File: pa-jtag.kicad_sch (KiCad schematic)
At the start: 25 parts, among them J1 USB_B, J2 JTAG, J3 VCCIO, J4 VOUT, U1 FT232RL, U2 L78L33_TO92

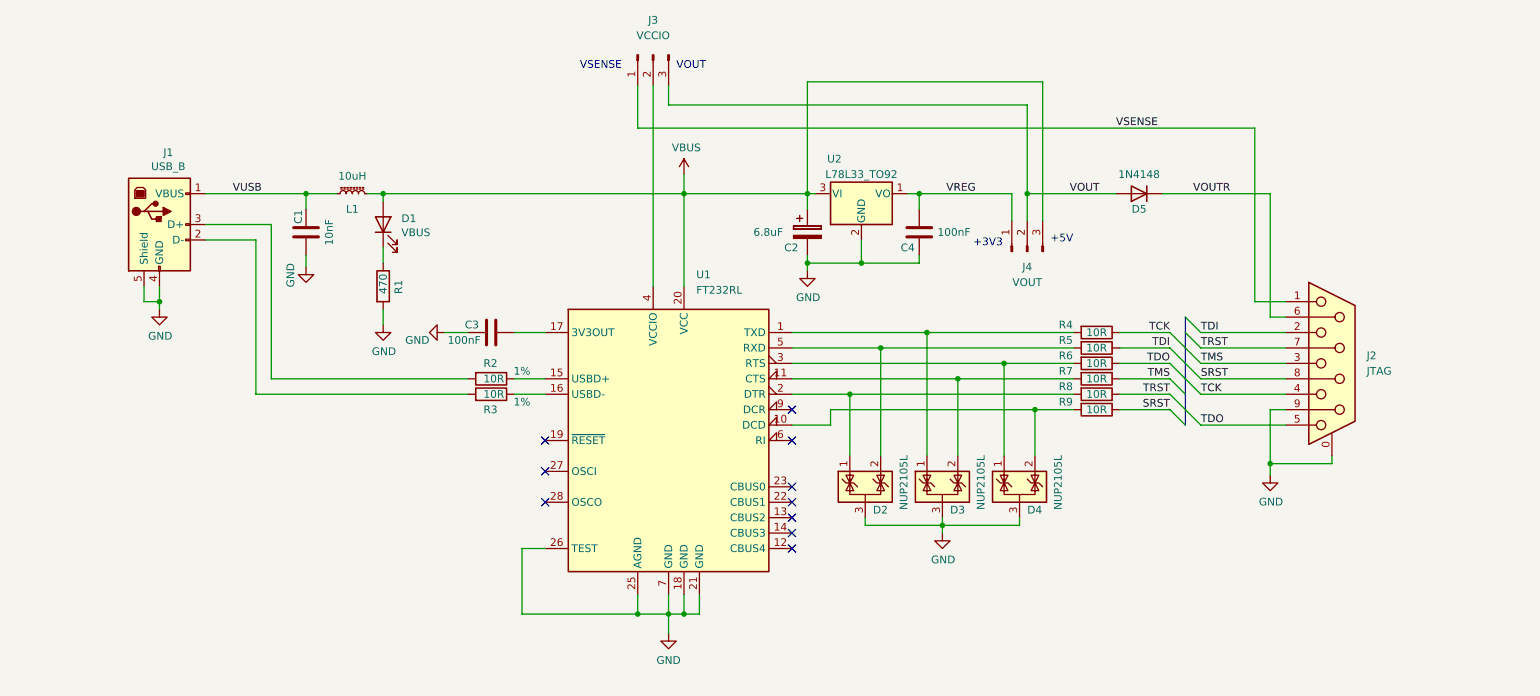
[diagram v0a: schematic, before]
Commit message: Add J5 and Open Drain Resets
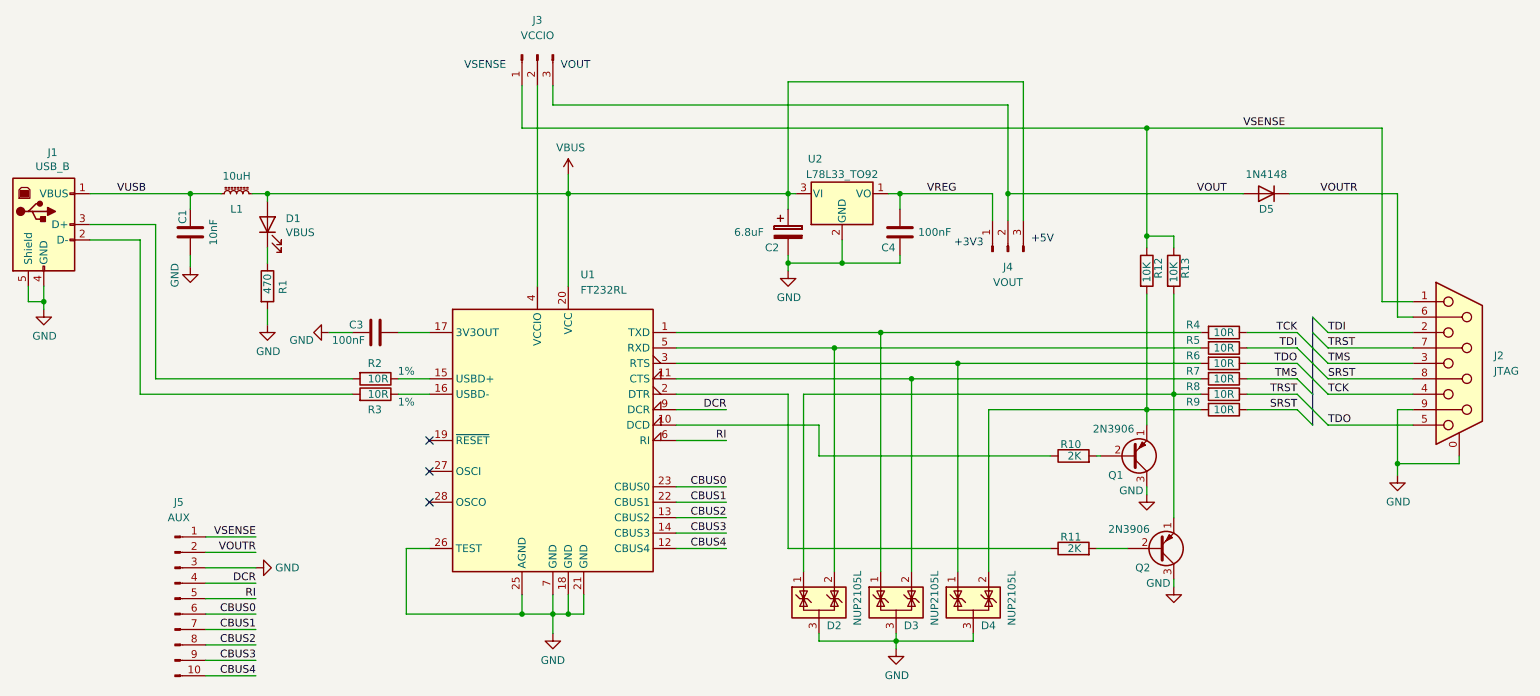
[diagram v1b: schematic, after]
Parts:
- added J5: AUX, Connector_PinHeader_2.54mm:PinHeader_2x05_P2.54mm_Vertical, symbol Connector:Conn_01x10_Male
- added Q1, Q2: 2N3906, Package_TO_SOT_THT:TO-92_Inline, symbol Transistor_BJT:2N3906
- added R10, R11: 2K, Resistor_SMD:R_0603_1608Metric, symbol Device:R
- added R12, R13: 10K, Resistor_SMD:R_0603_1608Metric, symbol Device:R
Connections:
- net GND: now also J5.3 (Pin_3), Q1.3 (C), Q2.3 (C)
- net VOUTR: now also J5.2 (Pin_2)
- net VSENSE: now also J5.1 (Pin_1), R12.1, R13.1
- net at D4.2 (K), R9.2: now also Q1.1 (E), R12.2; no longer U1.10 (DCD)
- net at D2.1 (K), R8.2: now also Q2.1 (E), R13.2; no longer U1.2 (DTR)
- net CBUS4: now reaches U1.12 (CBUS4)
- net CBUS4: now also J5.10 (Pin_10)
- net CBUS2: now reaches U1.13 (CBUS2)
- net CBUS2: now also J5.8 (Pin_8)
- net CBUS3: now reaches U1.14 (CBUS3)
- net CBUS3: now also J5.9 (Pin_9)
- net CBUS1: now reaches U1.22 (CBUS1)
- net CBUS1: now also J5.7 (Pin_7)
- net CBUS0: now reaches U1.23 (CBUS0)
- net CBUS0: now also J5.6 (Pin_6)
- net RI: now reaches U1.6 (RI)
- net RI: now also J5.5 (Pin_5)
- net DCR: now reaches U1.9 (DCR)
- net DCR: now also J5.4 (Pin_4)
- new net: R11.1, U1.2 (DTR)
- new net: Q2.2 (B), R11.2
- new net: R10.1, U1.10 (DCD)
- new net: Q1.2 (B), R10.2
- no-connect marks 10 -> 3
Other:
- moved on the sheet: C1, C2, C3, C4, D1, D2, D3, D4, D5, J1, J2, J3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

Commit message: ch32 initial commit
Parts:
- added C? (x4): 100nF, Capacitor_SMD:C_0603_1608Metric, symbol Device:C
- added U?: MAX3232, symbol Interface_UART:MAX3232
- added U?: CH32V103C8T6, Package_QFP:LQFP-48_7x7mm_P0.5mm, symbol MCU_ST_STM32F1:STM32F103C8Tx
- J2: value JTAG -> RS232
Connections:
- net CBUS0: no longer U1.23 (CBUS0)
- net CBUS1: no longer U1.22 (CBUS1)
- net CBUS2: no longer U1.13 (CBUS2)
- net CBUS3: no longer U1.14 (CBUS3)
- net CBUS4: no longer U1.12 (CBUS4)
- net DCR: no longer U1.9 (DCR)
- net GND: now also C?.2, C?.2, C?.2, C?.2, U?.23 (VSS), U?.35 (VSS), U?.47 (VSS), U?.8 (VSSA); no longer J2.0 (PAD), J2.9, U1.18 (GND), U1.21 (GND), U1.25 (AGND), U1.26 (TEST), U1.7 (GND)
- net RI: no longer U1.6 (RI)
- net SRST: no longer J2.8
- net TCK: no longer J2.4
- net TDI: no longer J2.2
- net TDO: no longer J2.5
- net TMS: no longer J2.3
- net TRST: no longer J2.7
- net VBUS: now also C3.1, C?.1, C?.1, C?.1, C?.1, U?.1 (VBAT), U?.24 (VDD), U?.36 (VDD), U?.48 (VDD), U?.9 (VDDA); no longer U1.20 (VCC)
- net VOUTR: no longer J2.6
- net VSENSE: no longer J2.1
- net at D3.1 (K), R4.2: no longer U1.1 (TXD)
- net at D3.2 (K), R7.2: no longer U1.11 (CTS)
- net at D4.1 (K), R6.2: no longer U1.3 (RTS)
- net at D2.2 (K), R5.2: no longer U1.5 (RXD)
- net at U1.17 (3V3OUT): no longer C3.1
- net at R2.1: no longer U1.15 (USBD+)
- net at R3.1: no longer U1.16 (USBD-)
- net at R11.1: no longer U1.2 (DTR)
- net at U1.4 (VCCIO): no longer J3.2 (Pin_2)
- net at R10.1: no longer U1.10 (DCD)
- new net VCCIO: J3.2 (Pin_2)
- no-connect marks 3 -> 0
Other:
- note added: "LEVEL SHIFTER"
- moved on the sheet: C1, C2, C3, C4, D1, D2, D3, D4, D5, J1, J2, J3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

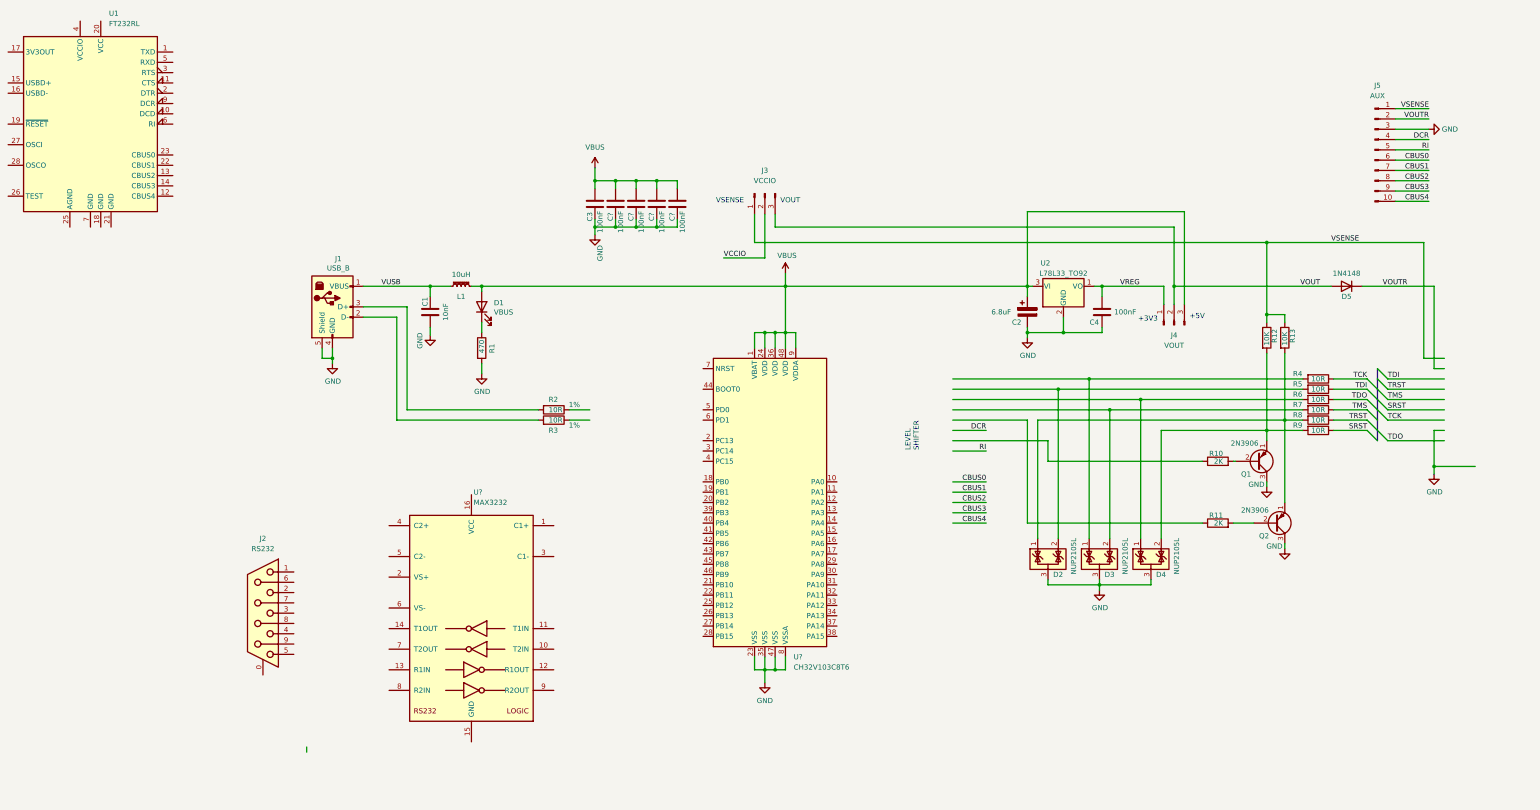
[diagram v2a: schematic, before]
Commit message: ch32v103 jtag schematic
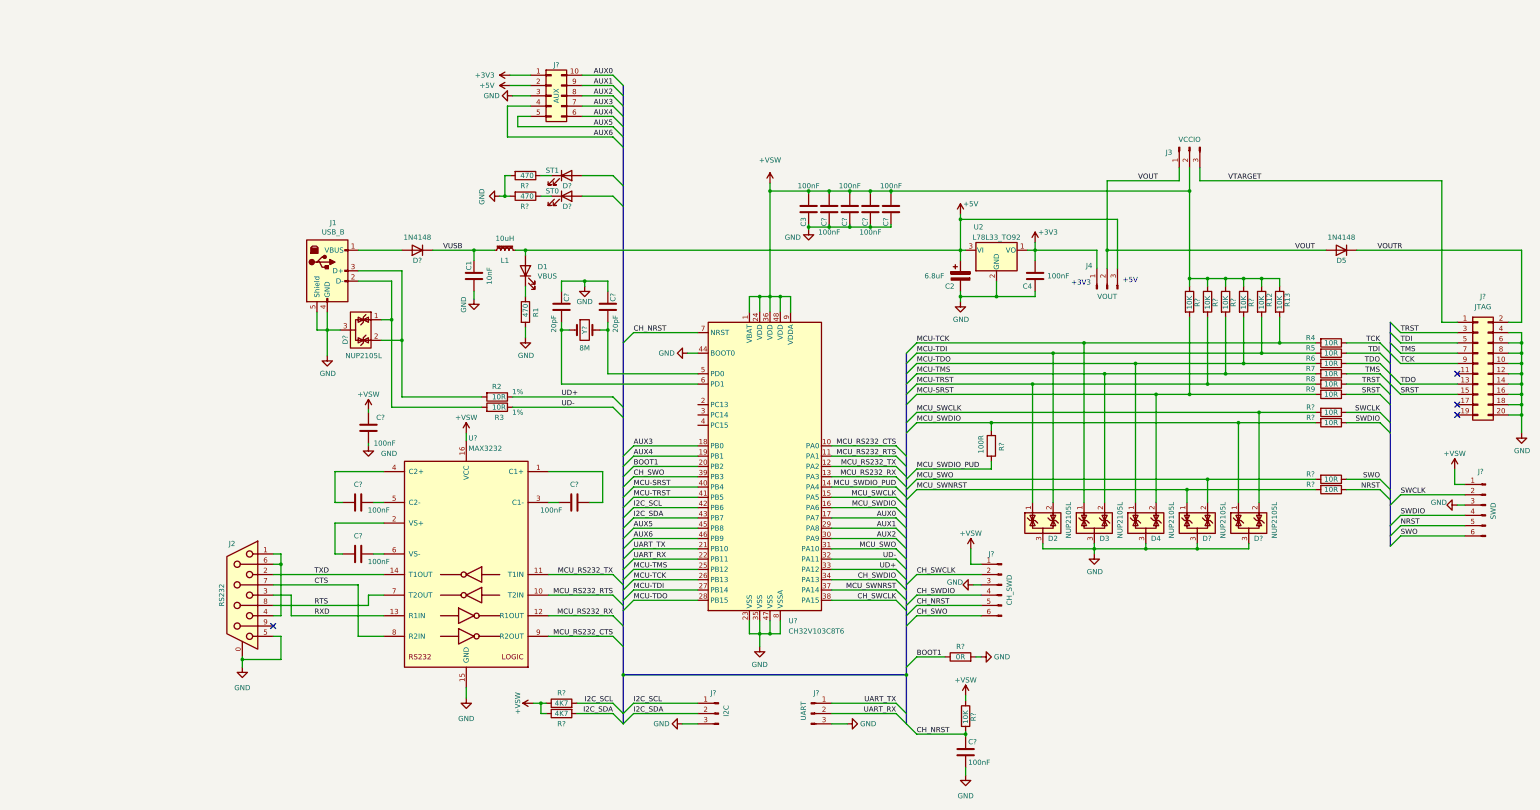
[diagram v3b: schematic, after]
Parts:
- removed J5: AUX, Connector_PinHeader_2.54mm:PinHeader_2x05_P2.54mm_Vertical, symbol Connector:Conn_01x10_Male
- removed Q1, Q2: 2N3906, Package_TO_SOT_THT:TO-92_Inline, symbol Transistor_BJT:2N3906
- removed R10, R11: 2K, Resistor_SMD:R_0603_1608Metric, symbol Device:R
- removed U1: FT232RL, Package_SO:SSOP-28_5.3x10.2mm_P0.65mm, symbol Interface_USB:FT232RL
- added C? (x5): 100nF, symbol Device:C
- added C? (x2): 20pF, symbol Device:C
- added D? (x3): NUP2105L, Package_TO_SOT_SMD:SOT-23, symbol Power_Protection:NUP2105L
- added D?: ST1, LED_SMD:LED_0603_1608Metric, symbol Device:LED
- added D?: 1N4148, Diode_SMD:D_MiniMELF, symbol Device:D
- added D?: ST0, LED_SMD:LED_0603_1608Metric, symbol Device:LED
- added J?: UART, symbol Connector:Conn_01x03_Male
- added J?: I2C, symbol Connector:Conn_01x03_Male
- added J?: CH_SWD, symbol Connector:Conn_01x06_Male
- added J?: AUX, symbol Connector_Generic:Conn_02x05_Counter_Clockwise
- added J?: SWD, symbol Connector:Conn_01x06_Male
- added J?: JTAG, symbol Connector_Generic:Conn_02x10_Odd_Even
- added R? (x2): 470, Resistor_SMD:R_0603_1608Metric, symbol Device:R
- added R?: 100R, symbol Device:R
- added R?: 0R, symbol Device:R
- added R? (x2): 4K7, symbol Device:R
- added R? (x4): 10R, Resistor_SMD:R_0603_1608Metric, symbol Device:R
- added R? (x4): 10K, Resistor_SMD:R_0603_1608Metric, symbol Device:R
- added R?: 10K, symbol Device:R
- added Y?: 8M, symbol Device:Crystal
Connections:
- net VCCIO is gone; now on net +VSW: J3.2 (Pin_2)
- net GND: now also J2.0 (PAD), J2.5, U?.15 (GND), U?.44 (BOOT0), C?.1, C?.1, C?.2, C?.2, D?.3 (A), D?.3 (A), D?.3 (A), J?.10 (Pin_10), J?.12 (Pin_12), J?.14 (Pin_14), J?.16 (Pin_16), J?.18 (Pin_18), J?.20 (Pin_20), J?.3 (Pin_3), J?.3 (Pin_3), J?.3 (Pin_3), J?.3 (Pin_3), J?.3 (Pin_3), J?.4 (Pin_4), J?.6 (Pin_6), J?.8 (Pin_8), R?.2, R?.2, R?.2
- net SRST: now also J?.15 (Pin_15)
- net TCK: now also J?.9 (Pin_9)
- net TDI: now also J?.5 (Pin_5)
- net TDO: now also J?.13 (Pin_13)
- net TMS: now also J?.7 (Pin_7)
- net TRST: now also J?.3 (Pin_3)
- net VOUT: now also J3.1 (Pin_1); no longer J3.3 (Pin_3)
- net VOUTR: now also J?.2 (Pin_2)
- net VUSB: now also D?.1 (K); no longer J1.1 (VBUS)
- net MCU-TCK: now reaches D3.1 (K), R4.2
- net MCU-TCK: now also R13.2, U?.26 (PB13)
- net MCU-TMS: now reaches D3.2 (K), R7.2
- net MCU-TMS: now also U?.25 (PB12), R?.2
- net at J1.2 (D-), R3.2: now also D?.1 (K)
- net at J1.3 (D+), R2.2: now also D?.2 (K)
- net MCU-TDO: now reaches D4.1 (K), R6.2
- net MCU-TDO: now also U?.28 (PB15), R?.2
- net MCU-SRST: now reaches D4.2 (K), R9.2
- net MCU-SRST: now also U?.40 (PB4), R?.2; no longer R12.2
- net MCU-TRST: now reaches D2.1 (K), R8.2
- net MCU-TRST: now also U?.41 (PB5), R?.2; no longer R13.2
- net MCU-TDI: now reaches D2.2 (K), R5.2
- net MCU-TDI: now also R12.2, U?.27 (PB14)
- net UD+: now reaches R2.1
- net UD+: now also U?.33 (PA12)
- net UD-: now reaches R3.1
- net UD-: now also U?.32 (PA11)
- net at U?.1 (C1+): now also C?.2
- net MCU_RS232_RTS: now reaches U?.10 (T2IN)
- net MCU_RS232_RTS: now also U?.11 (PA1)
- net MCU_RS232_TX: now reaches U?.11 (T1IN)
- net MCU_RS232_TX: now also U?.12 (PA2)
- net MCU_RS232_RX: now reaches U?.12 (R1OUT)
- net MCU_RS232_RX: now also U?.13 (PA3)
- net RXD: now reaches U?.13 (R1IN)
- net RXD: now also J2.3
- net TXD: now reaches U?.14 (T1OUT)
- net TXD: now also J2.2
- net +VSW: now reaches U?.16 (VCC)
- net +VSW: now also C3.1, C?.1, C?.1, C?.1, C?.1, R12.1, R13.1, U?.1 (VBAT), U?.24 (VDD), U?.36 (VDD), U?.48 (VDD), U?.9 (VDDA), C?.1, J?.1 (Pin_1), J?.1 (Pin_1), R?.1, R?.1, R?.1, R?.1, R?.1, R?.1, R?.1
- net at U?.2 (VS+): now also C?.1
- net at U?.3 (C1-): now also C?.1
- net at U?.4 (C2+): now also C?.1
- net at U?.5 (C2-): now also C?.2
- net at U?.6 (VS-): now also C?.2
- net RTS: now reaches U?.7 (T2OUT)
- net RTS: now also J2.8
- net CTS: now reaches U?.8 (R2IN)
- net CTS: now also J2.7
- net MCU_RS232_CTS: now reaches U?.9 (R2OUT)
- net MCU_RS232_CTS: now also U?.10 (PA0)
- net at J2.1: now also J2.4, J2.6
- net MCU_SWDIO_PUD: now reaches U?.14 (PA4)
- net MCU_SWDIO_PUD: now also R?.2
- net MCU_SWCLK: now reaches U?.15 (PA5)
- net MCU_SWCLK: now also D?.2 (K), R?.2
- net MCU_SWDIO: now reaches U?.16 (PA6)
- net MCU_SWDIO: now also D?.1 (K), R?.1, R?.2
- net AUX0: now reaches U?.17 (PA7)
- net AUX0: now also J?.10 (Pin_10)
- net AUX3: now reaches U?.18 (PB0)
- net AUX3: now also J?.7 (Pin_7)
- net AUX4: now reaches U?.19 (PB1)
- net AUX4: now also J?.6 (Pin_6)
- net BOOT1: now reaches U?.20 (PB2)
- net BOOT1: now also R?.1
- net UART_TX: now reaches U?.21 (PB10)
- net UART_TX: now also J?.1 (Pin_1)
- net UART_RX: now reaches U?.22 (PB11)
- net UART_RX: now also J?.2 (Pin_2)
- net AUX1: now reaches U?.29 (PA8)
- net AUX1: now also J?.9 (Pin_9)
- net AUX2: now reaches U?.30 (PA9)
- net AUX2: now also J?.8 (Pin_8)
- net MCU_SWO: now reaches U?.31 (PA10)
- net MCU_SWO: now also D?.2 (K), R?.2
- net CH_SWDIO: now reaches U?.34 (PA13)
- net CH_SWDIO: now also J?.4 (Pin_4)
- net MCU_SWNRST: now reaches U?.37 (PA14)
- net MCU_SWNRST: now also D?.1 (K), R?.2
- net CH_SWCLK: now reaches U?.38 (PA15)
- net CH_SWCLK: now also J?.2 (Pin_2)
- net CH_SWO: now reaches U?.39 (PB3)
- net CH_SWO: now also J?.6 (Pin_6)
- net I2C_SCL: now reaches U?.42 (PB6)
- net I2C_SCL: now also J?.1 (Pin_1), R?.2
- net I2C_SDA: now reaches U?.43 (PB7)
- net I2C_SDA: now also J?.2 (Pin_2), R?.2
- net AUX5: now reaches U?.45 (PB8)
- net AUX5: now also J?.5 (Pin_5)
- net AUX6: now reaches U?.46 (PB9)
- net AUX6: now also J?.4 (Pin_4)
- net at U?.5 (PD0): now also C?.2, Y?.2
- net at U?.6 (PD1): now also C?.2, Y?.1
- net CH_NRST: now reaches U?.7 (NRST)
- net CH_NRST: now also C?.1, J?.5 (Pin_5), R?.2
- removed net VBUS: C2.1, C3.1, C?.1, C?.1, C?.1, C?.1, D1.2 (A), J4.3 (Pin_3), L1.2, U2.3 (VI), U?.1 (VBAT), U?.24 (VDD), U?.36 (VDD), U?.48 (VDD), U?.9 (VDDA)
- net VREG renamed +3V3
- net +3V3: now also J?.1 (Pin_1)
- removed net VSENSE: J3.1 (Pin_1), R12.1, R13.1
- new net: D?.2 (A), J1.1 (VBUS)
- new net: D?.1 (K), R?.1 (x2)
- new net +5V: C2.1, D1.2 (A), J4.3 (Pin_3), J?.2 (Pin_2), L1.2, U2.3 (VI)
- new net NRST: J?.5 (Pin_5), R?.1
- new net SWCLK: J?.2 (Pin_2), R?.1
- new net SWDIO: J?.4 (Pin_4), R?.1
- new net SWO: J?.6 (Pin_6), R?.1
- new net VTARGET: J3.3 (Pin_3), J?.1 (Pin_1)
- no-connect marks 0 -> 4
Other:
- note removed: "LEVEL SHIFTER"
- note removed: "VOUT"
- note removed: "VSENSE"
- title: FT232R USB TO JTAG -> HIGH SPEED USB TO JTAG / SWD / UART / I2S / GPIO
- moved on the sheet: C1, C2, C3, C4, C?, D1, D2, D3, D4, D5, J1, J2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
